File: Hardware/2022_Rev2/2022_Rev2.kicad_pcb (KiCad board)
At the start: 2 copper layers, 132 parts, among them Q1 BUK768R3-60E, Q10 BUK768R3-60E, Q2 BUK768R3-60E, Q3 BUK768R3-60E, Q4 BUK768R3-60E, Q5 BUK768R3-60E, Q6 BUK768R3-60E, Q7 BUK768R3-60E, Q8 BUK768R3-60E, Q9 BUK768R3-60E, U1 OKI-78SR-5_1.5-W36-C, U10 LT1910, U11 LT1910, U12 LT1910, U13 INA281, U14 INA281, U15 INA281, U16 INA281, U17 LT1910, U18 INA281, U19 LT1910, U2 OKI-78SR-3.3_1.5-W36-C, U20 LT1910, U21 LT1910, U22 INA281, U23 INA281, U24 INA281, U3 OKI-78SR-5_1.5-W36-C, U4 OKI-78SR-5_1.5-W36-C, U5 LT1910, U6 LT1910, U7 INA281, U8 INA281, U9 LT1910

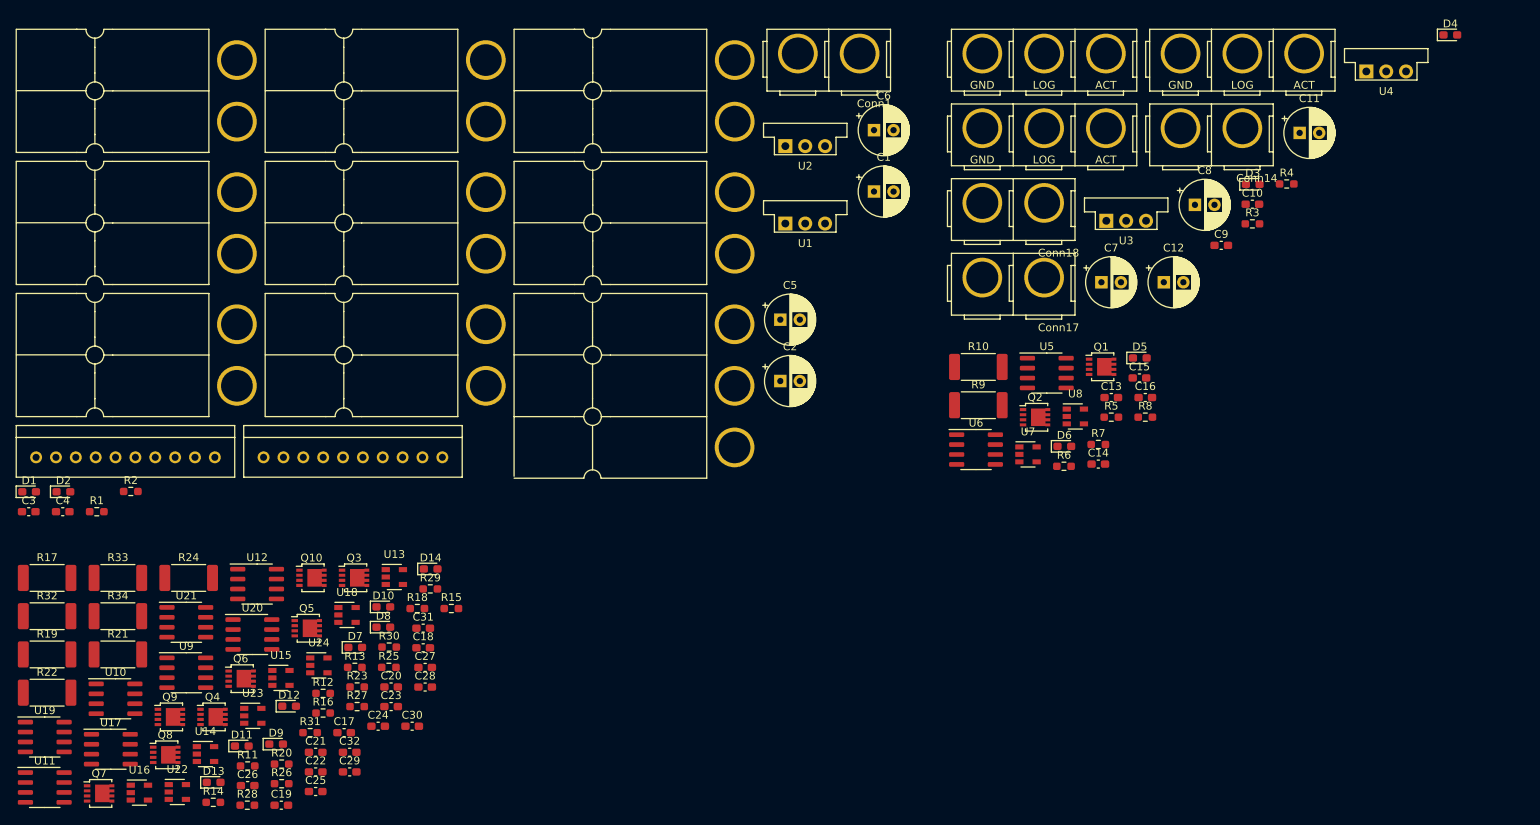
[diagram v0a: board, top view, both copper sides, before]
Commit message: fixed footprints
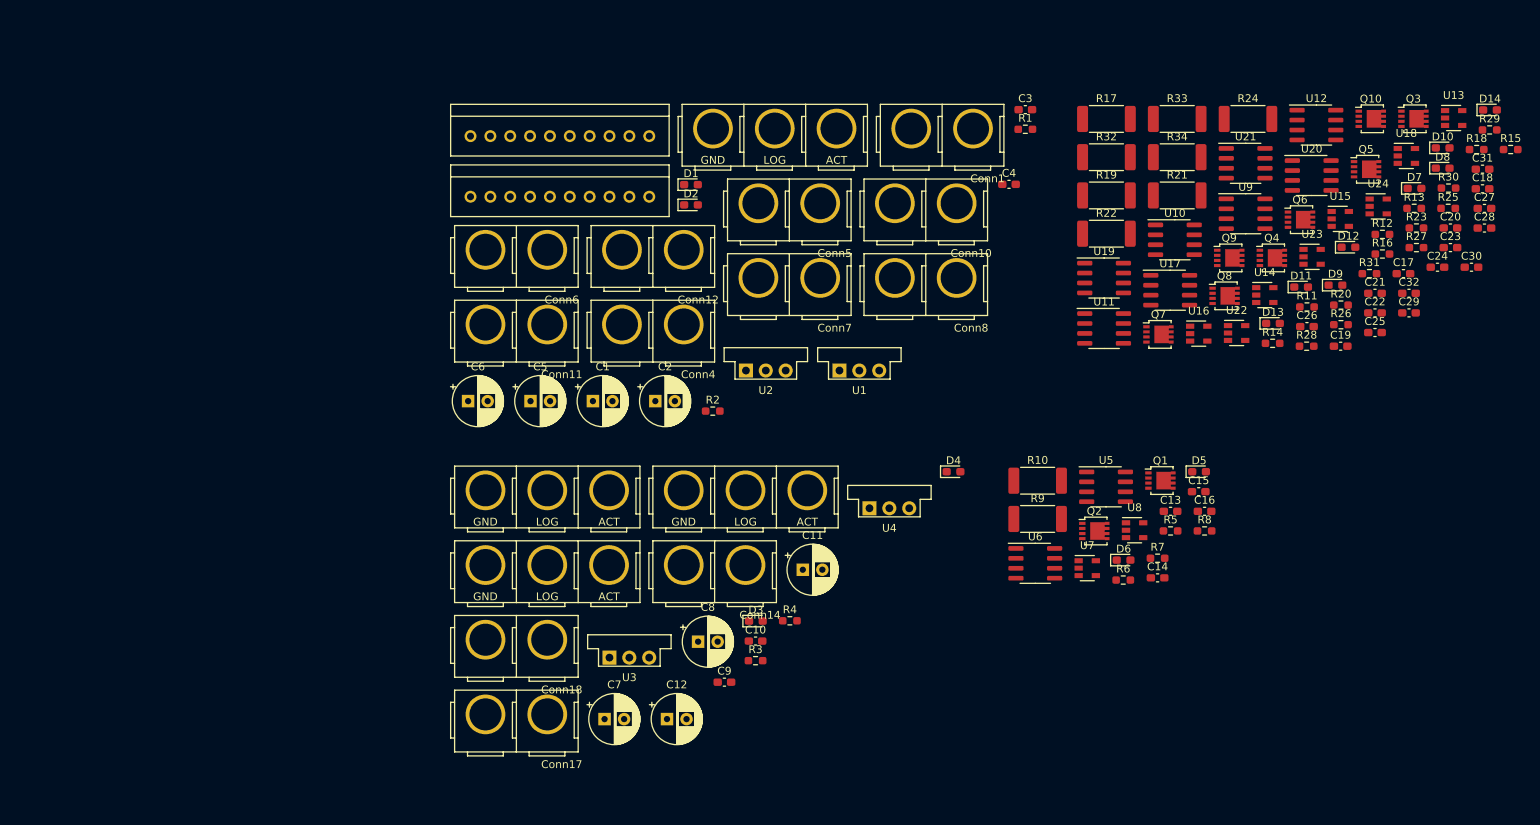
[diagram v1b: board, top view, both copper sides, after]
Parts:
- Conn10, Conn11, Conn12, Conn4, Conn5, Conn6, Conn7, Conn8: footprint MRDT_Connectors:Anderson_2_Horizontal_Side_by_Side_PV -> MRDT_Connectors:Anderson_2_Vertical_Sidy_by_Side
- Conn9: footprint MRDT_Connectors:Anderson_3_Horizontal_Side_by_Side -> MRDT_Connectors:Anderson_3_Vertical_Side_by_Side
- moved C17 147.6 mm to (489.2, 67.1)
- moved C18 147.6 mm to (499.3, 56.3)
- moved C19 147.6 mm to (481.2, 76.4)
- moved C20 147.6 mm to (495.2, 61.3)
- moved C21 147.6 mm to (485.6, 69.6)
- moved C22 147.6 mm to (485.6, 72.2)
- moved C23 147.6 mm to (495.2, 63.8)
- moved C24 147.6 mm to (493.6, 66.3)
- moved C25 147.6 mm to (485.6, 74.7)
- moved C26 147.6 mm to (476.9, 73.9)
- moved C27 147.6 mm to (499.6, 58.8)
- moved C28 147.6 mm to (499.6, 61.3)
- moved C29 147.6 mm to (489.9, 72.2)
- moved C30 147.6 mm to (497.9, 66.3)
- moved C31 147.6 mm to (499.3, 53.8)
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
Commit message: Gerbs are done
please review before you order this max
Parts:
- removed C10, C16, C3, C32, C4, C9: 10uF, Capacitor_SMD:C_0603_1608Metric_Pad1.08x0.95mm_HandSolder
- removed C11, C12, C5, C6: 47uF, Capacitor_THT:CP_Radial_D6.3mm_P2.50mm
- removed C13, C20: 0.1uF, Capacitor_SMD:C_0603_1608Metric_Pad1.08x0.95mm_HandSolder
- removed C7, C8: 22uF, Capacitor_THT:CP_Radial_D6.3mm_P2.50mm
- removed Conn14: Aux_GP_In, MRDT_Connectors:Anderson_2_Vertical_Sidy_by_Side
- removed Conn15: Aux_1_Out, MRDT_Connectors:Anderson_3_Vertical_Side_by_Side
- removed Conn16: Aux_2_Out, MRDT_Connectors:Anderson_3_Vertical_Side_by_Side
- removed Conn17: Aux_1_In, MRDT_Connectors:Anderson_2_Vertical_Sidy_by_Side
- removed Conn18: Aux_2_In, MRDT_Connectors:Anderson_2_Vertical_Sidy_by_Side
- removed D3, D4, D5: LED, Diode_SMD:D_0603_1608Metric_Pad1.05x0.95mm_HandSolder
- removed Q10, Q9: BUK768R3-60E, Package_TO_SOT_SMD:LFPAK33
- removed R12, R5, R6: 5.1k, Resistor_SMD:R_0603_1608Metric_Pad0.98x0.95mm_HandSolder
- removed R20, R7, R8: 330, Resistor_SMD:R_0603_1608Metric_Pad0.98x0.95mm_HandSolder
- removed R4: 510, Resistor_SMD:R_0603_1608Metric_Pad0.98x0.95mm_HandSolder
- removed R9: 0.0025, Resistor_SMD:R_2512_6332Metric_Pad1.40x3.35mm_HandSolder
- removed U10, U5, U6: LT1910, Package_SO:SOIC-8_3.9x4.9mm_P1.27mm
- removed U14, U7: INA281, Package_TO_SOT_SMD:SOT-23-5
- removed U3, U4: OKI-78SR-5_1.5-W36-C, Converter_DCDC:Converter_DCDC_muRata_OKI-78SR_Vertical
- added F1: 5A, MRDT_Passives:ATC_Fuse_Block, F.Cu at (170.9, 72.0)
- added F6: 5A, MRDT_Passives:ATC_Fuse_Block, F.Cu at (143.8, 72.0)
- added F8: 5A, MRDT_Passives:ATC_Fuse_Block, F.Cu at (196.1, 72.0)
- added F9: 5A, MRDT_Passives:ATC_Fuse_Block, F.Cu at (117.7, 72.0)
- added G***: LOGO, MRDT_Silkscreens:z_sig_Alex_Wortmann_PT2, F.Cu at (80.8, 96.5)
- added G***: LOGO, MRDT_Silkscreens:z_sig_Alex_Wortmann_PT1, F.Cu at (84.1, 87.9)
- added R35: 0.003, Resistor_SMD:R_2010_5025Metric_Pad1.52x2.65mm_HandSolder, F.Cu at (183.4, 52.6)
- added R36: 0.003, Resistor_SMD:R_2010_5025Metric_Pad1.52x2.65mm_HandSolder, F.Cu at (230.6, 52.3)
- added REF**: 4_40_Hole, MRDT_Drill_Holes:4_40_Hole, F.Cu at (70.6, 24.4)
- added REF**: 4_40_Hole, MRDT_Drill_Holes:4_40_Hole, F.Cu at (242.6, 24.4)
- added REF**: 4_40_Hole, MRDT_Drill_Holes:4_40_Hole_Corner, F.Cu at (230.6, 139.2)
- added REF**: 4_40_Hole, MRDT_Drill_Holes:4_40_Hole_Corner, F.Cu at (82.5, 139.2)
- added U25: INA281, Package_TO_SOT_SMD:SOT-23-5, F.Cu at (226.8, 52.3)
- added VR1: Q36SR12020NRFA, MRDT_Devices:Q36SR12020NRFA, F.Cu at (90.2, 120.7)
- added VR2: Q36SR12020NRFA, MRDT_Devices:Q36SR12020NRFA, F.Cu at (153.7, 120.7)
- C1: value 22uF -> 10uF; footprint Capacitor_THT:CP_Radial_D6.3mm_P2.50mm -> Capacitor_SMD:C_0603_1608Metric_Pad1.05x0.95mm_HandSolder
- C14, C17, C21, C22, C27, C28, C30, C31: footprint Capacitor_SMD:C_0603_1608Metric_Pad1.08x0.95mm_HandSolder -> Capacitor_SMD:C_0603_1608Metric_Pad1.05x0.95mm_HandSolder
- C15, C23, C24, C26: value 10uF -> 0.1uF; footprint Capacitor_SMD:C_0603_1608Metric_Pad1.08x0.95mm_HandSolder -> Capacitor_SMD:C_0603_1608Metric_Pad1.05x0.95mm_HandSolder
- C18, C19, C25, C29: value 0.1uF -> 10uF; footprint Capacitor_SMD:C_0603_1608Metric_Pad1.08x0.95mm_HandSolder -> Capacitor_SMD:C_0603_1608Metric_Pad1.05x0.95mm_HandSolder
- C2: footprint Capacitor_THT:CP_Radial_D6.3mm_P2.50mm -> Capacitor_SMD:C_0603_1608Metric_Pad1.05x0.95mm_HandSolder
- Conn1: value AndersonPP -> Molex_SL_09; footprint MRDT_Connectors:Anderson_2_Vertical_Side_by_Side_PV -> MRDT_Connectors:MOLEX_SL_09_Horizontal
- Conn10: value AndersonPP -> Nav; footprint MRDT_Connectors:Anderson_2_Vertical_Sidy_by_Side -> MRDT_Connectors:Square_Anderson_2_H_Stacked_PV
- Conn11: value AndersonPP -> Network Switch; footprint MRDT_Connectors:Anderson_2_Vertical_Sidy_by_Side -> MRDT_Connectors:Square_Anderson_2_H_Stacked_PV
- Conn12: value AndersonPP -> Multimedia; footprint MRDT_Connectors:Anderson_2_Vertical_Sidy_by_Side -> MRDT_Connectors:Square_Anderson_3_H_Side_By_Side
- Conn13: value Aux_GP_Out -> Molex_SL_09; footprint MRDT_Connectors:Anderson_3_Vertical_Side_by_Side -> MRDT_Connectors:MOLEX_SL_09_Horizontal
- Conn2: value Molex_SL_10 -> Pack; footprint MRDT_Connectors:MOLEX_SL_10_Vertical -> MRDT_Connectors:Square_Anderson_2_H_Stacked
- Conn3: value Molex_SL_10 -> Spare; footprint MRDT_Connectors:MOLEX_SL_10_Vertical -> MRDT_Connectors:Square_Anderson_3_H_Side_By_Side
- Conn4: value AndersonPP -> Aux; footprint MRDT_Connectors:Anderson_2_Vertical_Sidy_by_Side -> MRDT_Connectors:Square_Anderson_3_H_Side_By_Side
- Conn5: value AndersonPP -> BBB; footprint MRDT_Connectors:Anderson_2_Vertical_Sidy_by_Side -> MRDT_Connectors:Square_Anderson_2_H_Stacked_PV
- Conn6: value AndersonPP -> Cam1; footprint MRDT_Connectors:Anderson_2_Vertical_Sidy_by_Side -> MRDT_Connectors:Square_Anderson_2_H_Stacked_PV
- Conn7: value AndersonPP -> Cam2; footprint MRDT_Connectors:Anderson_2_Vertical_Sidy_by_Side -> MRDT_Connectors:Square_Anderson_2_H_Stacked_PV
- Conn8: value AndersonPP -> Drive; footprint MRDT_Connectors:Anderson_2_Vertical_Sidy_by_Side -> MRDT_Connectors:Square_Anderson_2_H_Stacked_PV
- Conn9: value AndersonPP -> Gimbal; footprint MRDT_Connectors:Anderson_3_Vertical_Side_by_Side -> MRDT_Connectors:Square_Anderson_3_H_Side_By_Side
- Q1, Q3, Q8: value BUK768R3-60E -> IRLML2803TRPBF; footprint Package_TO_SOT_SMD:LFPAK33 -> Package_TO_SOT_SMD:SOT-23
- Q2, Q4, Q5, Q6, Q7: value BUK768R3-60E -> FDC855N; footprint Package_TO_SOT_SMD:LFPAK33 -> Package_TO_SOT_SMD:SuperSOT-6
- R1: value 510 -> 330; footprint Resistor_SMD:R_0603_1608Metric_Pad0.98x0.95mm_HandSolder -> Resistor_SMD:R_0603_1608Metric_Pad1.05x0.95mm_HandSolder
- R10, R22: value 0.0025 -> 5.1k; footprint Resistor_SMD:R_2512_6332Metric_Pad1.40x3.35mm_HandSolder -> Resistor_SMD:R_0603_1608Metric_Pad1.05x0.95mm_HandSolder
- R11, R13, R27, R28: footprint Resistor_SMD:R_0603_1608Metric_Pad0.98x0.95mm_HandSolder -> Resistor_SMD:R_0603_1608Metric_Pad1.05x0.95mm_HandSolder
- R14, R25: value 5.1k -> 1k; footprint Resistor_SMD:R_0603_1608Metric_Pad0.98x0.95mm_HandSolder -> Resistor_SMD:R_0603_1608Metric_Pad1.05x0.95mm_HandSolder
- R15, R31: value 330 -> 1k; footprint Resistor_SMD:R_0603_1608Metric_Pad0.98x0.95mm_HandSolder -> Resistor_SMD:R_0603_1608Metric_Pad1.05x0.95mm_HandSolder
- R16, R18, R23: value 330 -> 0.003; footprint Resistor_SMD:R_0603_1608Metric_Pad0.98x0.95mm_HandSolder -> Resistor_SMD:R_2010_5025Metric_Pad1.52x2.65mm_HandSolder
- R17, R19, R24, R32, R33: value 0.0025 -> 1k; footprint Resistor_SMD:R_2512_6332Metric_Pad1.40x3.35mm_HandSolder -> Resistor_SMD:R_0603_1608Metric_Pad1.05x0.95mm_HandSolder
- R2: value 330 -> 0.0015; footprint Resistor_SMD:R_0603_1608Metric_Pad0.98x0.95mm_HandSolder -> Resistor_SMD:R_2512_6332Metric_Pad1.52x3.35mm_HandSolder
- R21, R34: value 0.0025 -> 0.003; footprint Resistor_SMD:R_2512_6332Metric_Pad1.40x3.35mm_HandSolder -> Resistor_SMD:R_2010_5025Metric_Pad1.52x2.65mm_HandSolder
- R26: value 5.1k -> 0.003; footprint Resistor_SMD:R_0603_1608Metric_Pad0.98x0.95mm_HandSolder -> Resistor_SMD:R_2010_5025Metric_Pad1.52x2.65mm_HandSolder
- R29, R30: value 330 -> 5.1k; footprint Resistor_SMD:R_0603_1608Metric_Pad0.98x0.95mm_HandSolder -> Resistor_SMD:R_0603_1608Metric_Pad1.05x0.95mm_HandSolder
- R3: value 510 -> 1k; footprint Resistor_SMD:R_0603_1608Metric_Pad0.98x0.95mm_HandSolder -> Resistor_SMD:R_0603_1608Metric_Pad1.05x0.95mm_HandSolder
- U1: value OKI-78SR-5_1.5-W36-C -> TSR1-2433; footprint Converter_DCDC:Converter_DCDC_muRata_OKI-78SR_Vertical -> MRDT_Devices:TSR_1-2433
- U12, U19: value LT1910 -> INA281; footprint Package_SO:SOIC-8_3.9x4.9mm_P1.27mm -> Package_TO_SOT_SMD:SOT-23-5
- U18, U22, U8: value INA281 -> LT1910; footprint Package_TO_SOT_SMD:SOT-23-5 -> Package_SO:SOIC-8_3.9x4.9mm_P1.27mm
- U2: value OKI-78SR-3.3_1.5-W36-C -> INA281; footprint Converter_DCDC:Converter_DCDC_muRata_OKI-78SR_Vertical -> Package_TO_SOT_SMD:SOT-23-5
- moved C29 381.7 mm to (108.7, 53.6), turned to 180 degrees
- moved U23 367.5 mm to (110.5, 46.2), turned to 90 degrees
- moved C26 367.0 mm to (110.0, 63.2), turned to 180 degrees
- moved U20 365.7 mm to (111.8, 58.4), turned to 90 degrees
- moved C18 364.7 mm to (134.6, 53.6), turned to 180 degrees
- moved Q6 363.8 mm to (112.3, 52.3), turned to 90 degrees
- moved R28 363.5 mm to (113.5, 63.2), turned to 180 degrees
- moved R16 346.8 mm to (140.2, 46.7), turned to 90 degrees
- moved R34 346.2 mm to (114.2, 46.5), turned to 90 degrees
- moved U12 341.7 mm to (136.4, 46.7), turned to 90 degrees
- moved C24 330.3 mm to (163.3, 63.2), turned to 180 degrees
- moved R31 326.7 mm to (159.0, 90.2), turned to 270 degrees
- moved R25 325.8 mm to (170.7, 90.2), turned to 270 degrees
- moved C14 324.7 mm to (135.9, 63.2), turned to 180 degrees
- moved C22 324.3 mm to (161.8, 53.6), turned to 180 degrees
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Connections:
- C1 pad 1: PV -> +12VA
- C15 pad 1: 12VA -> Net-(C15-Pad1)
- C19 pad 1: Net-(C19-Pad1) -> +12VA
- C2 pad 1: PV -> +5V
- C21 pad 1: Net-(C21-Pad1) -> +12VA
- C30 pad 1: Net-(C30-Pad1) -> Net-(C25-Pad1)
- C31 pad 1: Net-(C31-Pad1) -> +12VA
- Conn1 pad 1: GND -> Current_Sense_Aux
- Conn1 pad 4: PV -> Current_Sense_Cam2
- Conn10 pad 1: /12V/Anderson_Nav -> GND
- Conn10 pad 2: (no net) -> /12V/Anderson_Nav
- Conn11 pad 1: /12V/Anderson_NetSwitch -> GND
- Conn11 pad 2: (no net) -> +12VA
- Conn12 pad 1: /12V/Anderson_Multi -> GND
- Conn12 pad 2: (no net) -> /12V/Anderson_MultiAct
- Conn13 pad 1: GND -> Driver_Spare
- Conn13 pad 2: /BucksAndersons/GP_Toggle -> Driver_Nav
- Conn13 pad 3: (no net) -> Driver_Multi
- Conn2 pad 1: Current_Sense_AuxLog -> GND
- Conn2 pad 4: Current_Sense_Cam2 -> +36V
- Conn3 pad 1: Driver_AuxLog -> GND
- Conn3 pad 2: Driver_BBB -> /12V/Anderson_Spare
- Conn3 pad 3: Driver_Cam1 -> /12V/Anderson_Spare
- Conn4 pad 1: /12V/Anderson_AuxLog -> GND
- Conn4 pad 2: /12V/Anderson_AuxLog -> Net-(Conn4-Pad2)
- Conn5 pad 1: /12V/Anderson_BBB -> GND
- Conn5 pad 2: (no net) -> /12V/Anderson_BBB
- Conn6 pad 1: /12V/Anderson_Cam1 -> GND
- Conn6 pad 2: (no net) -> /12V/Anderson_Cam1
- Conn7 pad 1: /12V/Anderson_Cam2 -> GND
- Conn7 pad 2: (no net) -> /12V/Anderson_Cam2
- Conn8 pad 1: /12V/Anderson_Drive -> GND
- Conn8 pad 2: (no net) -> /12V/Anderson_Drive
- Conn9 pad 1: /12V/Anderson_GimAct -> GND
- Q1 pad 2: Net-(Q1-Pad1) -> Net-(Q1-Pad2)
- Q1 pad 3: Net-(Q1-Pad1) -> +12VA
- Q2 pad 1: Net-(Q2-Pad1) -> Net-(C18-Pad1)
- Q2 pad 2: Net-(Q2-Pad1) -> Net-(C18-Pad1)
- Q2 pad 3: Net-(Q2-Pad1) -> Net-(Q2-Pad3)
- Q2 pad 5: 12VA -> Net-(C18-Pad1)
- Q3 pad 2: Net-(Q3-Pad1) -> Net-(Q3-Pad2)
- Q3 pad 3: Net-(Q3-Pad1) -> +12VA
- Q4 pad 1: Net-(Q4-Pad1) -> Net-(C22-Pad1)
- Q4 pad 2: Net-(Q4-Pad1) -> Net-(C22-Pad1)
- Q4 pad 3: Net-(Q4-Pad1) -> Net-(Q4-Pad3)
- Q5 pad 1: Net-(Q5-Pad1) -> Net-(C25-Pad1)
- Q5 pad 2: Net-(Q5-Pad1) -> Net-(C25-Pad1)
- Q5 pad 3: Net-(Q5-Pad1) -> Net-(Q5-Pad3)
- Q5 pad 5: Net-(C23-Pad1) -> Net-(C25-Pad1)
- Q6 pad 1: Net-(Q6-Pad1) -> Net-(C29-Pad1)
- Q6 pad 2: Net-(Q6-Pad1) -> Net-(C29-Pad1)
- Q6 pad 3: Net-(Q6-Pad1) -> Net-(Q6-Pad3)
- Q6 pad 5: Net-(C24-Pad1) -> Net-(C29-Pad1)
- Q7 pad 1: Net-(Q7-Pad1) -> Net-(C25-Pad1)
- Q7 pad 2: Net-(Q7-Pad1) -> Net-(C25-Pad1)
- Q7 pad 3: Net-(Q7-Pad1) -> Net-(Q7-Pad3)
- Q7 pad 5: Net-(C26-Pad1) -> Net-(C25-Pad1)
- Q8 pad 2: Net-(Q8-Pad1) -> Net-(Q8-Pad2)
- Q8 pad 3: Net-(Q8-Pad1) -> +12VA
- R10 pad 1: Net-(Q2-Pad1) -> +5V
- R10 pad 2: /12V/Anderson_GimAct -> Net-(R10-Pad2)
- R11 pad 1: 5V -> +5V
- R13 pad 1: 5V -> +5V
- R14 pad 1: 5V -> Net-(D6-Pad2)
- R14 pad 2: Net-(R14-Pad2) -> Net-(Q2-Pad4)
- R15 pad 2: Net-(Q3-Pad1) -> Net-(Q1-Pad2)
- R16 pad 1: Net-(D8-Pad2) -> Net-(Q2-Pad4)
- R16 pad 2: Net-(Q4-Pad1) -> /12V/Anderson_MultiAct
- R17 pad 1: Net-(Q3-Pad1) -> Net-(D8-Pad2)
- R17 pad 2: /12V/Anderson_Multi -> +12VA
- R18 pad 1: Net-(D9-Pad2) -> Net-(Q1-Pad2)
- R18 pad 2: Net-(Q5-Pad1) -> /12V/Anderson_Drive
- R19 pad 1: Net-(Q4-Pad1) -> Net-(D9-Pad2)
- R19 pad 2: /12V/Anderson_Drive -> Net-(Q3-Pad2)
- R2 pad 1: Net-(D2-Pad2) -> Net-(R2-Pad1)
- R2 pad 2: +3V3 -> Net-(Conn4-Pad2)
- R21 pad 1: Net-(Q5-Pad1) -> Net-(Q3-Pad2)
- R21 pad 2: /12V/Anderson_NetSwitch -> /12V/Anderson_BBB
- R22 pad 1: Net-(Q6-Pad1) -> +5V
- R22 pad 2: /12V/Anderson_BBB -> Net-(R22-Pad2)
- R23 pad 1: Net-(D11-Pad2) -> Net-(Q4-Pad4)
- R23 pad 2: Net-(Q7-Pad1) -> /12V/Anderson_Spare
- R24 pad 1: Net-(Q7-Pad1) -> Net-(D10-Pad2)
- R24 pad 2: /12V/Anderson_Cam2 -> Net-(Q5-Pad4)
- R25 pad 1: 5V -> Net-(D11-Pad2)
- R25 pad 2: Net-(R25-Pad2) -> Net-(Q4-Pad4)
- R26 pad 1: 5V -> Net-(Q5-Pad4)
- R26 pad 2: Net-(R26-Pad2) -> /12V/Anderson_Cam2
- R27 pad 1: 5V -> +5V
- R28 pad 1: 5V -> +5V
- R29 pad 1: Net-(D12-Pad2) -> +5V
- R29 pad 2: Net-(Q8-Pad1) -> Net-(R29-Pad2)
- R3 pad 1: Net-(D3-Pad2) -> Net-(D2-Pad2)
- R3 pad 2: /BucksAndersons/12VA -> Net-(R2-Pad1)
- R30 pad 1: Net-(D13-Pad2) -> +5V
- R30 pad 2: Net-(Q9-Pad1) -> Net-(R30-Pad2)
- R31 pad 1: Net-(D14-Pad2) -> Net-(D12-Pad2)
- R31 pad 2: Net-(Q10-Pad1) -> Net-(Q6-Pad4)
- R32 pad 1: Net-(Q8-Pad1) -> Net-(D13-Pad2)
- R32 pad 2: /12V/Anderson_GimAct -> Net-(Q7-Pad4)
- R33 pad 1: Net-(Q9-Pad1) -> Net-(D14-Pad2)
- R33 pad 2: /12V/Anderson_Cam1 -> Net-(Q8-Pad2)
- R34 pad 1: Net-(Q10-Pad1) -> Net-(Q6-Pad4)
- R34 pad 2: /12V/Anderson_Nav -> /12V/Anderson_GimAct
- U1 pad 1: PV -> +12VA
- U11 pad 2: Net-(C19-Pad1) -> Net-(C17-Pad1)
- U11 pad 4: Driver_NetSwitch -> Driver_BBB
- U11 pad 5: Net-(Q5-Pad4) -> Net-(Q3-Pad1)
- U11 pad 6: Net-(C23-Pad1) -> +12VA
- U11 pad 8: Net-(C23-Pad1) -> +12VA
- U12 pad 1: GND -> Current_Sense_Multi
- U12 pad 2: Net-(C20-Pad1) -> GND
- U12 pad 3: Net-(R14-Pad2) -> Net-(Q2-Pad4)
- U12 pad 4: Driver_BBB -> /12V/Anderson_MultiAct
- U12 pad 5: Net-(Q6-Pad4) -> +5V
- U13 pad 1: Current_Sense_Multi -> Current_Sense_Drive
- U13 pad 3: Net-(Q3-Pad1) -> Net-(Q1-Pad2)
- U13 pad 4: /12V/Anderson_Multi -> /12V/Anderson_Drive
- U13 pad 5: 5V -> +5V
- U15 pad 1: Current_Sense_NetSwitch -> Current_Sense_BBB
- U15 pad 3: Net-(Q5-Pad1) -> Net-(Q3-Pad2)
- U15 pad 4: /12V/Anderson_NetSwitch -> /12V/Anderson_BBB
- U15 pad 5: 5V -> +5V
- U16 pad 1: Current_Sense_BBB -> Current_Sense_Spare
- U16 pad 3: Net-(Q6-Pad1) -> Net-(Q4-Pad4)
- U16 pad 4: /12V/Anderson_BBB -> /12V/Anderson_Spare
- U16 pad 5: 5V -> +5V
- U17 pad 2: Net-(C25-Pad1) -> Net-(C24-Pad1)
- U17 pad 3: Net-(R25-Pad2) -> Net-(R22-Pad2)
- U17 pad 4: Driver_Cam2 -> Driver_Spare
- U17 pad 5: Net-(Q7-Pad4) -> Net-(Q4-Pad3)
- U17 pad 6: Net-(C26-Pad1) -> Net-(C22-Pad1)
- U17 pad 8: Net-(C26-Pad1) -> Net-(C22-Pad1)
- U18 pad 1: Current_Sense_Cam2 -> GND
- U18 pad 2: GND -> Net-(C23-Pad1)
- U18 pad 3: Net-(Q7-Pad1) -> Net-(R27-Pad2)
- U18 pad 4: /12V/Anderson_Cam2 -> Driver_Cam2
- U18 pad 5: 5V -> Net-(Q5-Pad3)
- U19 pad 1: GND -> Current_Sense_Cam2
- U19 pad 2: Net-(C27-Pad1) -> GND
- U19 pad 3: Net-(R26-Pad2) -> Net-(Q5-Pad4)
- U19 pad 4: Driver_GimLog -> /12V/Anderson_Cam2
- U19 pad 5: Net-(Q8-Pad4) -> +5V
- U2 pad 1: PV -> Current_Sense_Aux
- U2 pad 3: +3V3 -> Net-(R2-Pad1)
- U20 pad 2: Net-(C28-Pad1) -> Net-(C26-Pad1)
- U20 pad 3: Net-(R27-Pad2) -> Net-(R28-Pad2)
- U20 pad 4: Driver_Cam1 -> Driver_Gim
- U20 pad 5: Net-(Q9-Pad4) -> Net-(Q6-Pad3)
- U20 pad 6: Net-(C31-Pad1) -> Net-(C29-Pad1)
- U20 pad 8: Net-(C31-Pad1) -> Net-(C29-Pad1)
- U21 pad 2: Net-(C29-Pad1) -> Net-(C27-Pad1)
- U21 pad 3: Net-(R28-Pad2) -> Net-(R29-Pad2)
- U21 pad 4: Driver_Nav -> Driver_Cam1
- U21 pad 5: Net-(Q10-Pad4) -> Net-(Q7-Pad3)
- U21 pad 6: Net-(C32-Pad1) -> Net-(C25-Pad1)
- U21 pad 8: Net-(C32-Pad1) -> Net-(C25-Pad1)
- U22 pad 1: Current_Sense_GimLog -> GND
- U22 pad 2: GND -> Net-(C28-Pad1)
- U22 pad 3: Net-(Q8-Pad1) -> Net-(R30-Pad2)
- U22 pad 4: /12V/Anderson_GimAct -> Driver_Nav
- U22 pad 5: 5V -> Net-(Q8-Pad1)
- U23 pad 1: Current_Sense_Cam1 -> Current_Sense_Gim
- U23 pad 3: Net-(Q9-Pad1) -> Net-(Q6-Pad4)
- U23 pad 4: /12V/Anderson_Cam1 -> /12V/Anderson_GimAct
- U23 pad 5: 5V -> +5V
- U24 pad 1: Current_Sense_Nav -> Current_Sense_Cam1
- U24 pad 3: Net-(Q10-Pad1) -> Net-(Q7-Pad4)
- U24 pad 4: /12V/Anderson_Nav -> /12V/Anderson_Cam1
- U24 pad 5: 5V -> +5V
- U8 pad 1: Current_Sense_GimAct -> GND
- U8 pad 2: GND -> Net-(C14-Pad1)
- U8 pad 3: Net-(Q2-Pad1) -> Net-(R10-Pad2)
- U8 pad 4: /12V/Anderson_GimAct -> Driver_Multi
- U8 pad 5: 5V -> Net-(Q2-Pad3)
- U9 pad 2: Net-(C17-Pad1) -> Net-(C15-Pad1)
- U9 pad 4: Driver_Multi -> Driver_Drive
- U9 pad 5: Net-(Q3-Pad4) -> Net-(Q1-Pad1)
- U9 pad 6: Net-(C21-Pad1) -> +12VA
- U9 pad 8: Net-(C21-Pad1) -> +12VA
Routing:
- net +5V: track 0.00 -> 468.5 mm, vias 0 -> 10
- net Net-(Q6-Pad4): track 0.00 -> 303.3 mm, vias 0 -> 2
- net Net-(Q2-Pad4): track 0.00 -> 269.2 mm, vias 0 -> 2
- net Net-(Q4-Pad4): track 0.00 -> 235.3 mm, vias 0 -> 2
- net Current_Sense_Aux: track 0.00 -> 193.4 mm, vias 0 -> 4
- net Current_Sense_Gim: track 0.00 -> 180.1 mm, vias 0 -> 6
- net Driver_Multi: track 0.00 -> 178.5 mm, vias 0 -> 8
- net Driver_Aux: track 0.00 -> 167.0 mm, vias 0 -> 5
- net Driver_Gim: track 0.00 -> 161.1 mm, vias 0 -> 8
- net Current_Sense_Multi: track 0.00 -> 158.3 mm, vias 0 -> 10
- net Current_Sense_Spare: track 0.00 -> 116.4 mm, vias 0 -> 4
- net Driver_Spare: track 0.00 -> 102.9 mm, vias 0 -> 4
- net Net-(Q1-Pad2): track 0.00 -> 100.4 mm, vias 0 -> 4
- net Current_Sense_Cam1: track 0.00 -> 94.9 mm, vias 0 -> 4
- net Current_Sense_Cam2: track 0.00 -> 86.9 mm, vias 0 -> 4
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- added copper zone on F.Cu, net +12VA
- added copper zone on F.Cu, net +36V
- added copper zone on F.Cu, net /12V/Anderson_BBB
- added copper zone on F.Cu, net /12V/Anderson_Cam1
- added copper zone on F.Cu, net /12V/Anderson_Cam2
- added copper zone on F.Cu, net /12V/Anderson_Drive
- added copper zone on F.Cu, net /12V/Anderson_GimAct
- added copper zone on F.Cu, net /12V/Anderson_MultiAct
- added copper zone on F.Cu, net /12V/Anderson_Nav
- added copper zone on F.Cu, net /12V/Anderson_Spare
- added copper zone on B.Cu, net GND
- added copper zone on F.Cu, net GND
- added copper zone on F.Cu, net Net-(C18-Pad1)
- added copper zone on F.Cu, net Net-(C22-Pad1)
- added copper zone on F.Cu, net Net-(C25-Pad1)
- added copper zone on F.Cu, net Net-(C29-Pad1)
- added copper zone on F.Cu, net Net-(Conn4-Pad2)
- added copper zone on F.Cu, net Net-(Q1-Pad2)
- added copper zone on F.Cu, net Net-(Q2-Pad4)
- added copper zone on F.Cu, net Net-(Q3-Pad2)
- added copper zone on F.Cu, net Net-(Q4-Pad4)
- added copper zone on F.Cu, net Net-(Q5-Pad4)
- added copper zone on F.Cu, net Net-(Q6-Pad4)
- added copper zone on F.Cu, net Net-(Q7-Pad4)
- added copper zone on F.Cu, net Net-(Q8-Pad2)
- added copper zone on F.Cu, net Net-(R2-Pad1)
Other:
- board outline added: 180.1 x 127 mm
- board text added: "1"
- board text added: "10"
- board text added: "12V Distrobution Board Rev 2 Mars Rover Design Team Alex Wortmann"
- board text added: "2"
- board text added: "3"
- board text added: "4"
- board text added: "5"
- board text added: "5V Power"
- board text added: "6"
- board text added: "7"
- board text added: "8"
- board text added: "9"
- board text added: "Aux (20A)"
- board text added: "Blackbox"
- board text added: "Camera 1"
- board text added: "Camera 2"
- board text added: "Dan Napierkowski"
- board text added: "Drive Board"
- board text added: "Gimbal"
- board text added: "Multimedia"
- board text added: "Nav Board"
- board text added: "Net Switch"
- board text added: "Spare"

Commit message: changed board review complaints
generated gerbs
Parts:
- moved G*** 31.2 mm to (78.7, 57.1)
- moved G*** 31.2 mm to (75.4, 65.8)
- moved Conn1 8.00 mm to (233.4, 78.1)
- moved Conn13 8.00 mm to (233.4, 106.0)
- moved REF** 7.87 mm to (238.5, 139.2)
- moved REF** 7.87 mm to (74.7, 139.2)
- moved Conn2 7.76 mm to (228.1, 135.4)
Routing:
- net Current_Sense_Gim: track 180.1 -> 193.3 mm
- net Driver_Gim: track 161.1 -> 170.9 mm
- net Driver_Multi: track 178.5 -> 188.2 mm
- net Current_Sense_Aux: track 193.4 -> 203.1 mm
- net Current_Sense_Multi: track 158.3 -> 167.5 mm
- net Driver_Spare: track 102.9 -> 110.9 mm
- net Driver_Cam2: track 76.6 -> 84.6 mm
- net Driver_Cam1: track 86.6 -> 94.6 mm
- net Current_Sense_Spare: track 116.4 -> 124.4 mm
- net Current_Sense_Cam2: track 86.9 -> 94.9 mm
- net Current_Sense_Cam1: track 94.9 -> 102.9 mm
- net Current_Sense_BBB: track 40.9 -> 48.9 mm
- net Driver_Aux: track 167.0 -> 173.0 mm
- net Current_Sense_Drive: track 42.1 -> 46.0 mm
- net Driver_Drive: track 61.3 -> 64.2 mm, vias 4 -> 2
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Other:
- outline, holes or cut-outs redrawn
